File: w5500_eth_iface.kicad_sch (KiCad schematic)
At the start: 11 parts, among them U4 W5500, Y1 25MHz

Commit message: 10nF 0603: 1276-1921-1-ND -> 1276-1009-1-ND
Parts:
- C14: DigiKey Part Number 1276-1921-1-ND -> 1276-1009-1-ND
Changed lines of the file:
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@@
       (effects (font (size 1.27 1.27)) hide)
     )
-    (property "DigiKey Part Number" "1276-1921-1-ND" (id 4) (at 104.14 88.9 0)
+    (property "DigiKey Part Number" "1276-1009-1-ND" (id 4) (at 104.14 88.9 0)
       (effects (font (size 1.27 1.27)) hide)
     )

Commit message: w5500 crystal: CTX1437CT-ND -> CTX1175CT-ND
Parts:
- Y1: DigiKey Part Number CTX1437CT-ND -> CTX1175CT-ND
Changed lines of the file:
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@@
       (effects (font (size 1.27 1.27)) hide)
     )
-    (property "DigiKey Part Number" "CTX1437CT-ND" (id 4) (at 149.86 104.14 90)
+    (property "DigiKey Part Number" "CTX1175CT-ND" (id 4) (at 149.86 104.14 90)
       (effects (font (size 1.27 1.27)) hide)
     )

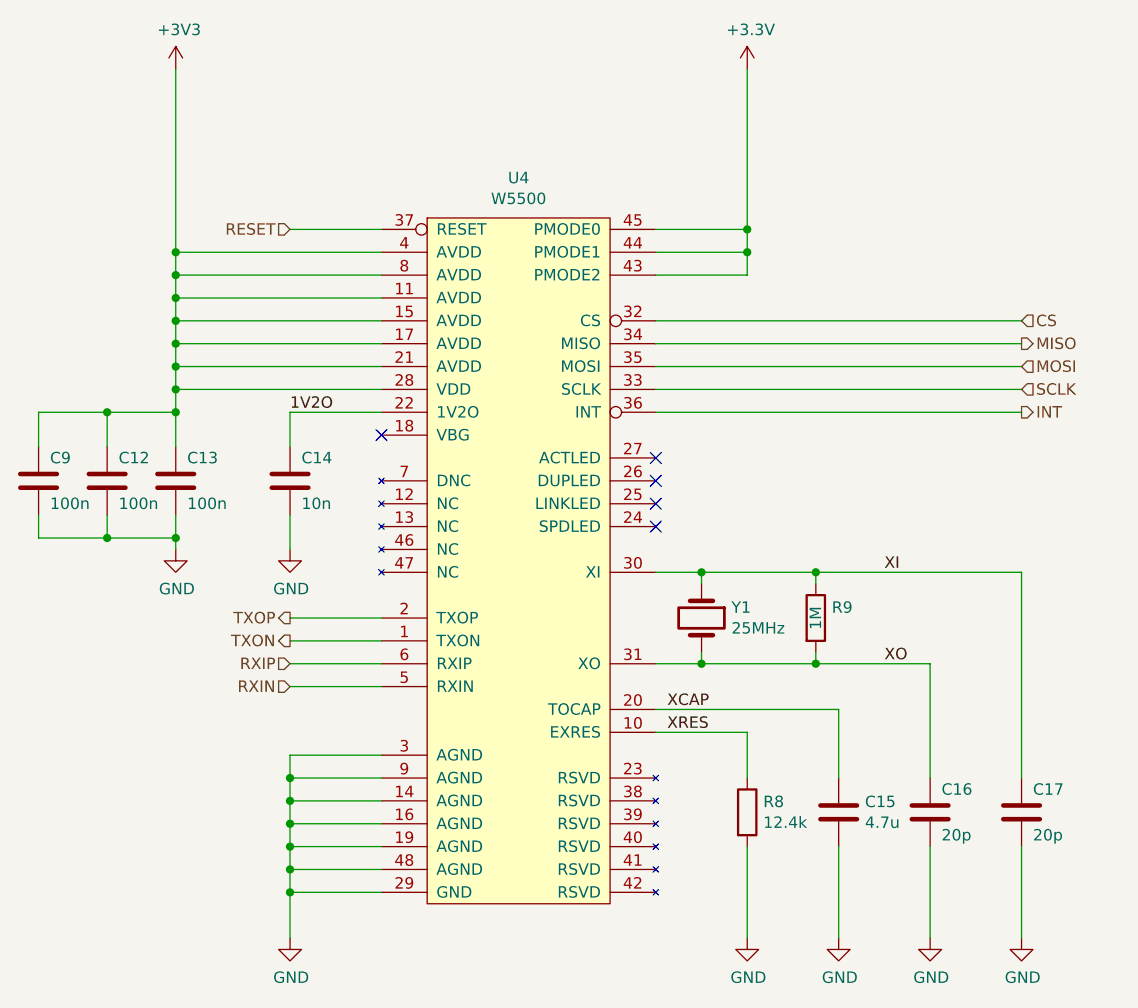
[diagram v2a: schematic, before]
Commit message: add mounting holes, replace magjack with in-stock part
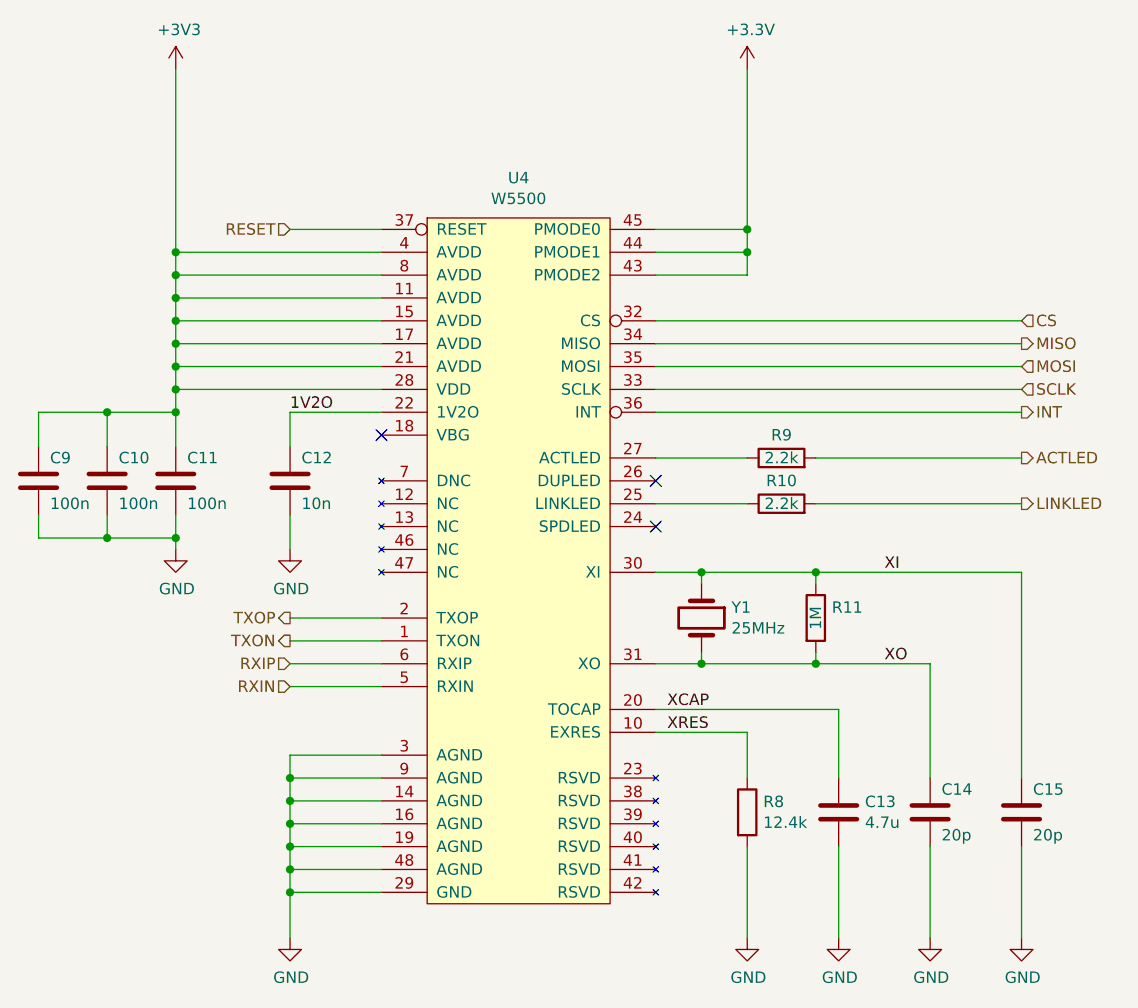
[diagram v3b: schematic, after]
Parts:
- added R10, R9: 2.2k, Resistor_SMD:R_0603_1608Metric, symbol Device:R
- renumbered C12 to C10, C13 to C11, C14 to C12, C15 to C13, C16 to C14, C17 to C15, R9 to R11
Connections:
- net at U4.25 (LINKLED): now also R10.1
- net at U4.27 (ACTLED): now also R9.1
- new net ACTLED: R9.2
- new net LINKLED: R10.2
- no-connect marks 5 -> 3
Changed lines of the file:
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@@
   (no_connect (at 144.78 88.9))
   (no_connect (at 144.78 93.98))
-  (no_connect (at 144.78 91.44))
   (no_connect (at 114.3 83.82))
-  (no_connect (at 144.78 86.36))
   (wire (pts (xy 165.1 139.7) (xy 165.1 129.54))
     (stroke (width 0) (type default) (color 0 0 0 0))
@@
     (stroke (width 0) (type default) (color 0 0 0 0))
   )
+  (wire (pts (xy 162.56 91.44) (xy 185.42 91.44))
+    (stroke (width 0) (type default) (color 0 0 0 0))
+  )
   (wire (pts (xy 91.44 73.66) (xy 91.44 76.2))
     (stroke (width 0) (type default) (color 0 0 0 0))
@@
     (stroke (width 0) (type default) (color 0 0 0 0))
   )
+  (wire (pts (xy 144.78 91.44) (xy 154.94 91.44))
+    (stroke (width 0) (type default) (color 0 0 0 0))
+  )
   (wire (pts (xy 114.3 81.28) (xy 104.14 81.28))
     (stroke (width 0) (type default) (color 0 0 0 0))
@@
     (stroke (width 0) (type default) (color 0 0 0 0))
   )
+  (wire (pts (xy 144.78 86.36) (xy 154.94 86.36))
+    (stroke (width 0) (type default) (color 0 0 0 0))
+  )
   (wire (pts (xy 91.44 96.52) (xy 91.44 95.25))
     (stroke (width 0) (type default) (color 0 0 0 0))
@@
   )
   (wire (pts (xy 76.2 92.71) (xy 76.2 95.25))
+    (stroke (width 0) (type default) (color 0 0 0 0))
+  )
+  (wire (pts (xy 162.56 86.36) (xy 185.42 86.36))
     (stroke (width 0) (type default) (color 0 0 0 0))
   )
@@
     (effects (font (size 1.27 1.27)) (justify right))
   )
+  (hierarchical_label "ACTLED" (shape output) (at 185.42 86.36 0)
+    (effects (font (size 1.27 1.27)) (justify left))
+  )
   (hierarchical_label "SCLK" (shape input) (at 185.42 78.74 0)
     (effects (font (size 1.27 1.27)) (justify left))
   )
+  (hierarchical_label "LINKLED" (shape output) (at 185.42 91.44 0)
+    (effects (font (size 1.27 1.27)) (justify left))
+  )
   (hierarchical_label "MOSI" (shape input) (at 185.42 76.2 0)
     (effects (font (size 1.27 1.27)) (justify left))
@@
   (symbol (lib_id "power:GND") (at 104.14 139.7 0) (unit 1)
     (in_bom yes) (on_board yes)
-    (property "Reference" "#PWR014" (id 0) (at 104.14 146.05 0)
+    (property "Reference" "#PWR015" (id 0) (at 104.14 146.05 0)
       (effects (font (size 1.27 1.27)) hide)
     )
@@
   (symbol (lib_id "power:GND") (at 154.94 139.7 0) (unit 1)
     (in_bom yes) (on_board yes)
-    (property "Reference" "#PWR016" (id 0) (at 154.94 146.05 0)
+    (property "Reference" "#PWR017" (id 0) (at 154.94 146.05 0)
       (effects (font (size 1.27 1.27)) hide)
     )
@@
   (symbol (lib_id "Device:C") (at 165.1 125.73 0) (unit 1)
     (in_bom yes) (on_board yes)
-    (property "Reference" "C15" (id 0) (at 168.021 124.5616 0)
+    (property "Reference" "C13" (id 0) (at 168.021 124.5616 0)
       (effects (font (size 1.27 1.27)) (justify left))
     )
@@
   (symbol (lib_id "power:GND") (at 165.1 139.7 0) (unit 1)
     (in_bom yes) (on_board yes)
-    (property "Reference" "#PWR017" (id 0) (at 165.1 146.05 0)
+    (property "Reference" "#PWR018" (id 0) (at 165.1 146.05 0)
       (effects (font (size 1.27 1.27)) hide)
     )
@@
   (symbol (lib_id "Device:R") (at 162.56 104.14 0) (unit 1)
     (in_bom yes) (on_board yes)
-    (property "Reference" "R9" (id 0) (at 164.338 102.9716 0)
+    (property "Reference" "R11" (id 0) (at 164.338 102.9716 0)
       (effects (font (size 1.27 1.27)) (justify left))
     )
@@
   (symbol (lib_id "Device:C") (at 104.14 88.9 0) (unit 1)
     (in_bom yes) (on_board yes)
-    (property "Reference" "C14" (id 0) (at 105.41 86.36 0)
+    (property "Reference" "C12" (id 0) (at 105.41 86.36 0)
       (effects (font (size 1.27 1.27)) (justify left))
     )
@@
   (symbol (lib_id "power:GND") (at 104.14 96.52 0) (unit 1)
     (in_bom yes) (on_board yes)
-    (property "Reference" "#PWR013" (id 0) (at 104.14 102.87 0)
+    (property "Reference" "#PWR014" (id 0) (at 104.14 102.87 0)
       (effects (font (size 1.27 1.27)) hide)
     )
@@
   (symbol (lib_id "power:GND") (at 91.44 96.52 0) (unit 1)
     (in_bom yes) (on_board yes)
-    (property "Reference" "#PWR012" (id 0) (at 91.44 102.87 0)
+    (property "Reference" "#PWR013" (id 0) (at 91.44 102.87 0)
       (effects (font (size 1.27 1.27)) hide)
     )
@@
   (symbol (lib_id "Device:C") (at 185.42 125.73 0) (unit 1)
     (in_bom yes) (on_board yes)
-    (property "Reference" "C17" (id 0) (at 186.69 123.19 0)
+    (property "Reference" "C15" (id 0) (at 186.69 123.19 0)
       (effects (font (size 1.27 1.27)) (justify left))
     )
@@
   (symbol (lib_id "power:GND") (at 175.26 139.7 0) (unit 1)
     (in_bom yes) (on_board yes)
-    (property "Reference" "#PWR018" (id 0) (at 175.26 146.05 0)
+    (property "Reference" "#PWR019" (id 0) (at 175.26 146.05 0)
       (effects (font (size 1.27 1.27)) hide)
     )
@@
   (symbol (lib_id "power:GND") (at 185.42 139.7 0) (unit 1)
     (in_bom yes) (on_board yes)
-    (property "Reference" "#PWR019" (id 0) (at 185.42 146.05 0)
+    (property "Reference" "#PWR020" (id 0) (at 185.42 146.05 0)
       (effects (font (size 1.27 1.27)) hide)
     )
@@
   (symbol (lib_id "power:+3.3V") (at 154.94 43.18 0) (unit 1)
     (in_bom yes) (on_board yes)
-    (property "Reference" "#PWR015" (id 0) (at 154.94 46.99 0)
+    (property "Reference" "#PWR016" (id 0) (at 154.94 46.99 0)
       (effects (font (size 1.27 1.27)) hide)
     )
@@
   (symbol (lib_id "power:+3V3") (at 91.44 43.18 0) (unit 1)
     (in_bom yes) (on_board yes)
-    (property "Reference" "#PWR011" (id 0) (at 91.44 46.99 0)
+    (property "Reference" "#PWR012" (id 0) (at 91.44 46.99 0)
       (effects (font (size 1.27 1.27)) hide)
     )
@@
   (symbol (lib_id "Device:C") (at 83.82 88.9 0) (unit 1)
     (in_bom yes) (on_board yes)
-    (property "Reference" "C12" (id 0) (at 85.09 86.36 0)
+    (property "Reference" "C10" (id 0) (at 85.09 86.36 0)
       (effects (font (size 1.27 1.27)) (justify left))
     )
@@
   (symbol (lib_id "Device:C") (at 91.44 88.9 0) (unit 1)
     (in_bom yes) (on_board yes)
-    (property "Reference" "C13" (id 0) (at 92.71 86.36 0)
+    (property "Reference" "C11" (id 0) (at 92.71 86.36 0)
       (effects (font (size 1.27 1.27)) (justify left))
     )
@@
     (pin "2")
   )
+  (symbol (lib_id "Device:R") (at 158.75 86.36 90) (unit 1)
+    (in_bom yes) (on_board yes)
+    (property "Reference" "R9" (id 0) (at 158.75 83.82 90))
+    (property "Value" "2.2k" (id 1) (at 158.75 86.36 90))
+    (property "Footprint" "Resistor_SMD:R_0603_1608Metric" (id 2) (at 158.75 88.138 90)
+      (effects (font (size 1.27 1.27)) hide)
+    )
+    (property "Datasheet" "~" (id 3) (at 158.75 86.36 0)
+      (effects (font (size 1.27 1.27)) hide)
+    )
+    (property "DigiKey Part Number" "311-2.20KHRCT-ND" (id 4) (at 158.75 86.36 0)
+      (effects (font (size 1.27 1.27)) hide)
+    )
+    (pin "1")
+    (pin "2")
+  )
   (symbol (lib_id "Device:C") (at 175.26 125.73 0) (unit 1)
     (in_bom yes) (on_board yes)
-    (property "Reference" "C16" (id 0) (at 176.53 123.19 0)
+    (property "Reference" "C14" (id 0) (at 176.53 123.19 0)
       (effects (font (size 1.27 1.27)) (justify left))
     )
@@
       (effects (font (size 1.27 1.27)) hide)
     )
+    (pin "1")
+    (pin "2")
+  )
+  (symbol (lib_id "Device:R") (at 158.75 91.44 90) (unit 1)
+    (in_bom yes) (on_board yes)
+    (property "Reference" "R10" (id 0) (at 158.75 88.9 90))
+    (property "Value" "2.2k" (id 1) (at 158.75 91.44 90))
+    (property "Footprint" "Resistor_SMD:R_0603_1608Metric" (id 2) (at 158.75 93.218 90)
+      (effects (font (size 1.27 1.27)) hide)
+    )
+    (property "Datasheet" "~" (id 3) (at 158.75 91.44 0)
+      (effects (font (size 1.27 1.27)) hide)
+    )
+    (property "DigiKey Part Number" "311-2.20KHRCT-ND" (id 4) (at 158.75 91.44 0)
+      (effects (font (size 1.27 1.27)) hide)
+    )
